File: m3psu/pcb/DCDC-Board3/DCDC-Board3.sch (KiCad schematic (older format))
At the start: 6 parts

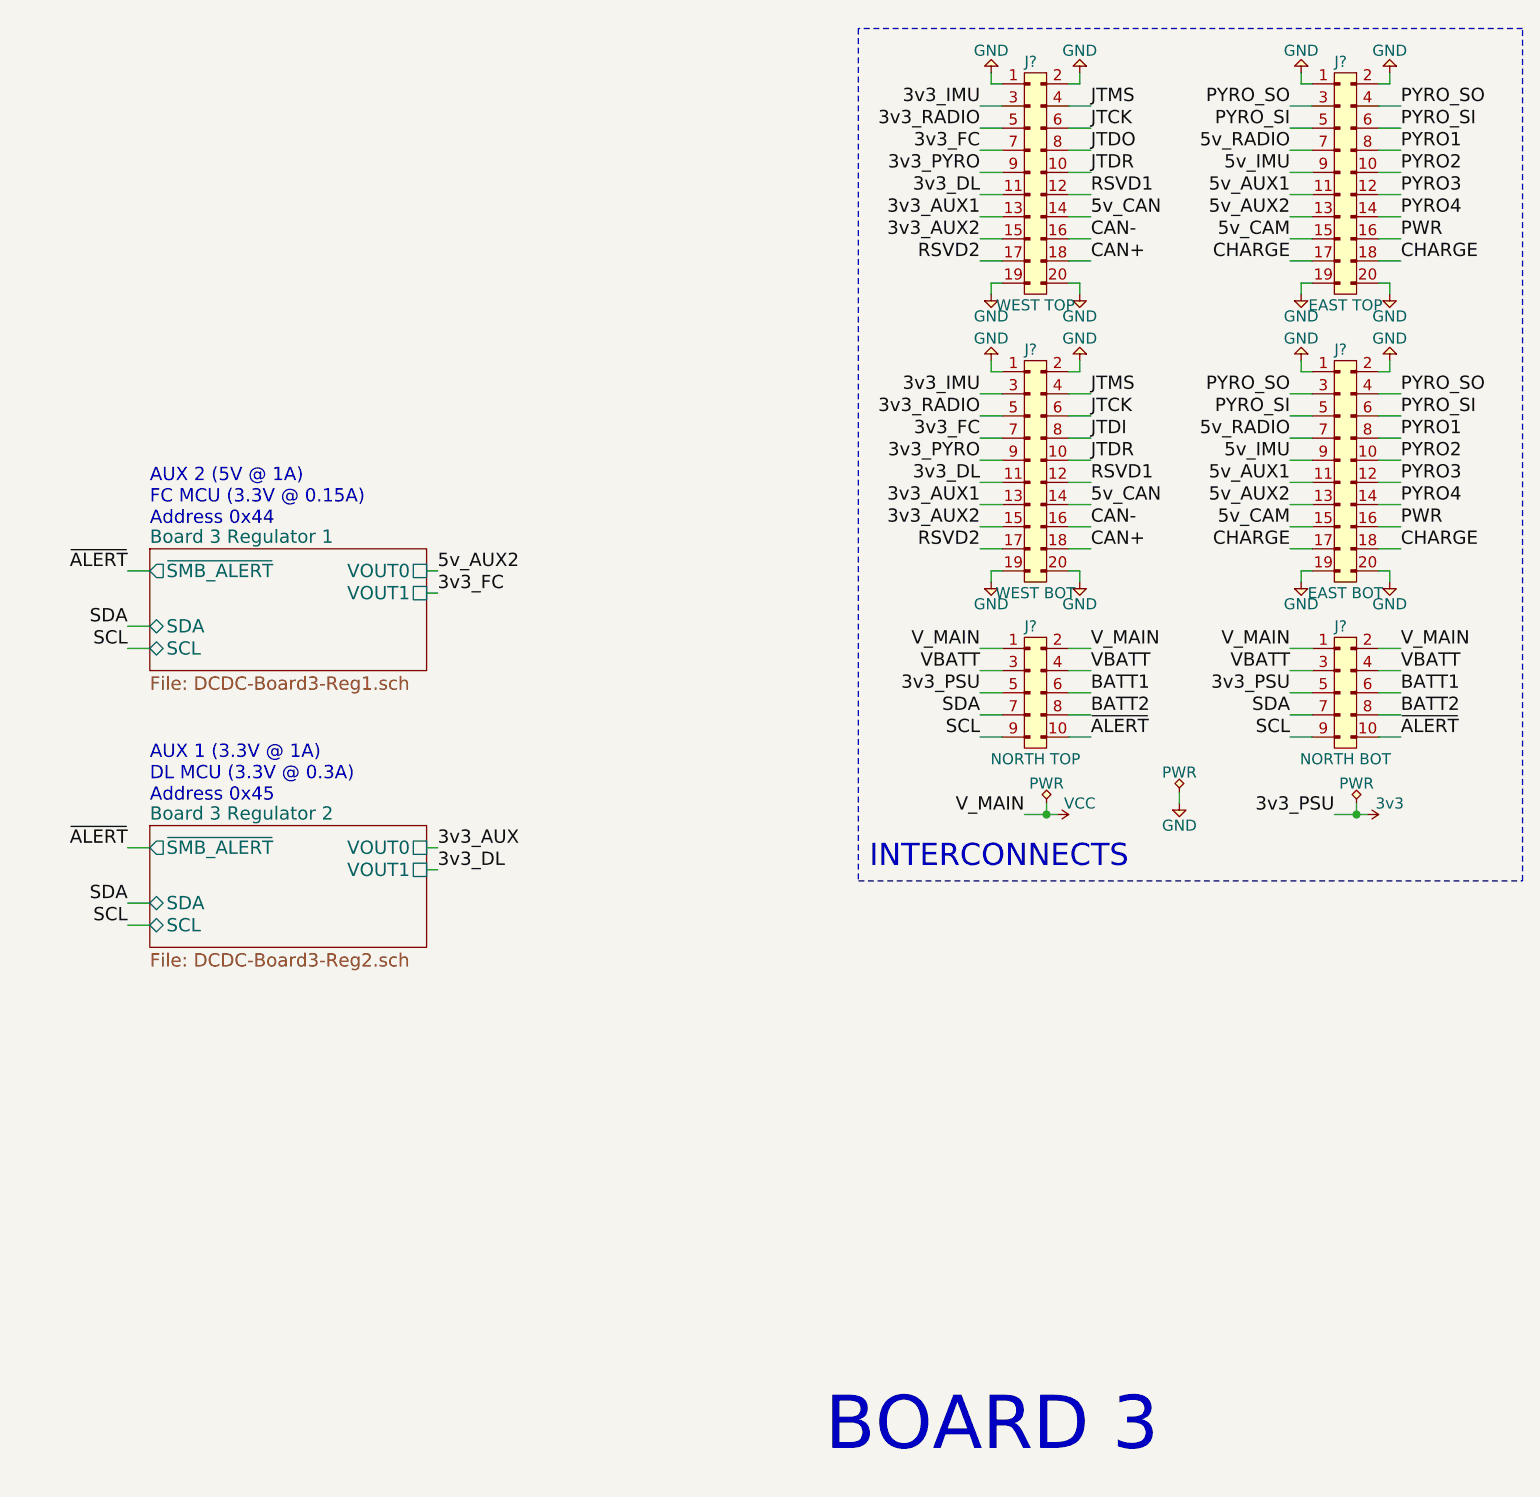
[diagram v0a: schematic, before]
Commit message: create DCDC1/2/3 from prototype
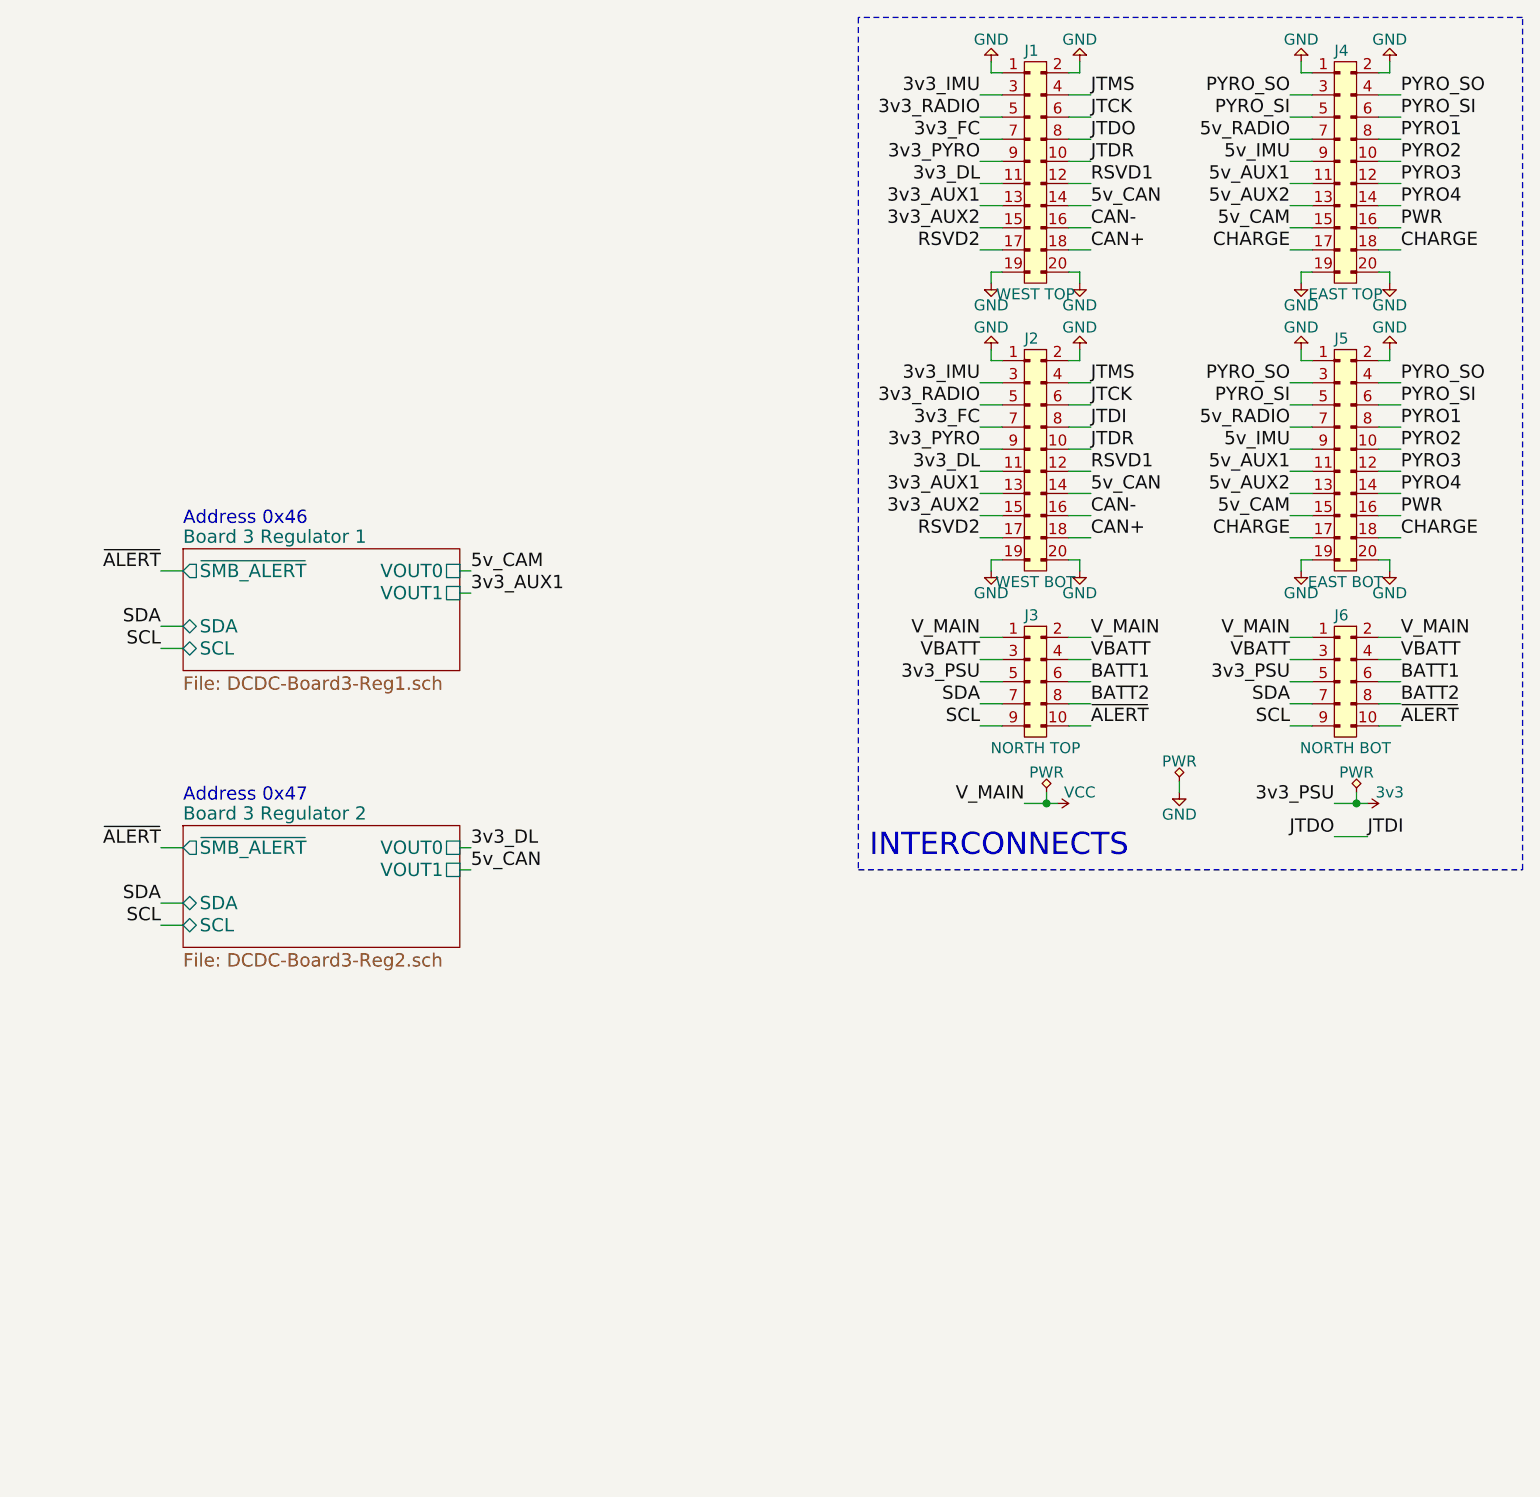
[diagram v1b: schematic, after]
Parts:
- removed J?: WEST TOP, agg:TFML-110-02-L-D, symbol CONN_02x10
- removed J?: EAST TOP, agg:TFML-110-02-L-D, symbol CONN_02x10
- removed J?: WEST BOT, agg:SFML-110-02-L-D-LC, symbol CONN_02x10
- removed J?: EAST BOT, agg:SFML-110-02-L-D-LC, symbol CONN_02x10
- removed J?: NORTH TOP, agg:SFML-105-02-L-D, symbol CONN_02x05
- removed J?: NORTH BOT, agg:SFML-105-02-L-D-LC, symbol CONN_02x05
- added J1: WEST TOP, agg:TFML-110-02-L-D, symbol CONN_02x10
- added J2: WEST BOT, agg:SFML-110-02-L-D-LC, symbol CONN_02x10
- added J3: NORTH TOP, agg:TFML-105-02-L-D, symbol CONN_02x05
- added J4: EAST TOP, agg:TFML-110-02-L-D, symbol CONN_02x10
- added J5: EAST BOT, agg:SFML-110-02-L-D-LC, symbol CONN_02x10
- added J6: NORTH BOT, agg:SFML-105-02-L-D-LC, symbol CONN_02x05
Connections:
- net 3v3: now also J3.5, J6.5
- net 3v3_AUX1: now also J1.13, J2.13
- net 3v3_AUX2: now also J1.15, J2.15
- net 3v3_DL: now also J1.11, J2.11
- net 3v3_FC: now also J1.7, J2.7
- net 3v3_IMU: now also J1.3, J2.3
- net 3v3_PYRO: now also J1.9, J2.9
- net 3v3_RADIO: now also J1.5, J2.5
- net 5v_AUX1: now also J4.11, J5.11
- net 5v_AUX2: now also J4.13, J5.13
- net 5v_CAM: now also J4.15, J5.15
- net 5v_CAN: now also J1.14, J2.14
- net 5v_IMU: now also J4.9, J5.9
- net 5v_RADIO: now also J4.7, J5.7
- net BATT1: now also J3.6, J6.6
- net BATT2: now also J3.8, J6.8
- net CAN+: now also J1.18, J2.18
- net CAN-: now also J1.16, J2.16
- net CHARGE: now also J4.17, J4.18, J5.17, J5.18
- net GND: now also J1.1, J1.19, J1.2, J1.20, J2.1, J2.19, J2.2, J2.20, J4.1, J4.19, J4.2, J4.20, J5.1, J5.19, J5.2, J5.20
- net JTCK: now also J1.6, J2.6
- net JTDI: now also J1.8, J2.8
- net JTDR: now also J1.10, J2.10
- net JTMS: now also J1.4, J2.4
- net PWR: now also J4.16, J5.16
- net PYRO1: now also J4.8, J5.8
- net PYRO2: now also J4.10, J5.10
- net PYRO3: now also J4.12, J5.12
- net PYRO4: now also J4.14, J5.14
- net PYRO_SI: now also J4.5, J4.6, J5.5, J5.6
- net PYRO_SO: now also J4.3, J4.4, J5.3, J5.4
- net RSVD1: now also J1.12, J2.12
- net RSVD2: now also J1.17, J2.17
- net SCL: now also J3.9, J6.9
- net SDA: now also J3.7, J6.7
- net VBATT: now also J3.3, J3.4, J6.3, J6.4
- net VCC: now also J3.1, J3.2, J6.1, J6.2
- net ~ALERT: now also J3.10, J6.10
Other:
- note added: "Address 0x46"
- note added: "Address 0x47"
- note removed: "AUX 1 (3.3V @ 1A)\nDL MCU (3.3V @ 0.3A)\nAddress 0x45"
- note removed: "AUX 2 (5V @ 1A)\nFC MCU (3.3V @ 0.15A)\nAddress 0x44"
- note removed: "BOARD 3"
